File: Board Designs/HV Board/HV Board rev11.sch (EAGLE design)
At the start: 73 parts, among them IC1 OKI-78SR-5, IC2 NE5532SOIC

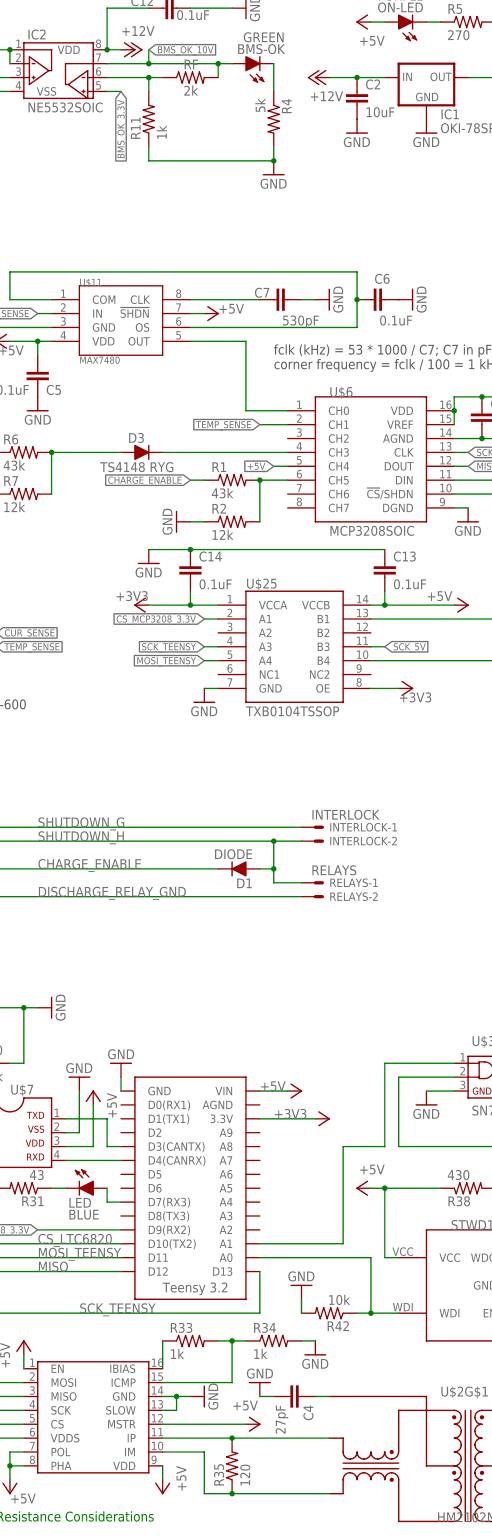
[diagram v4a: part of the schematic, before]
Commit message: HV Board rev11: comp hardware - removed extra isoSPI resistor, changed LED resistor value
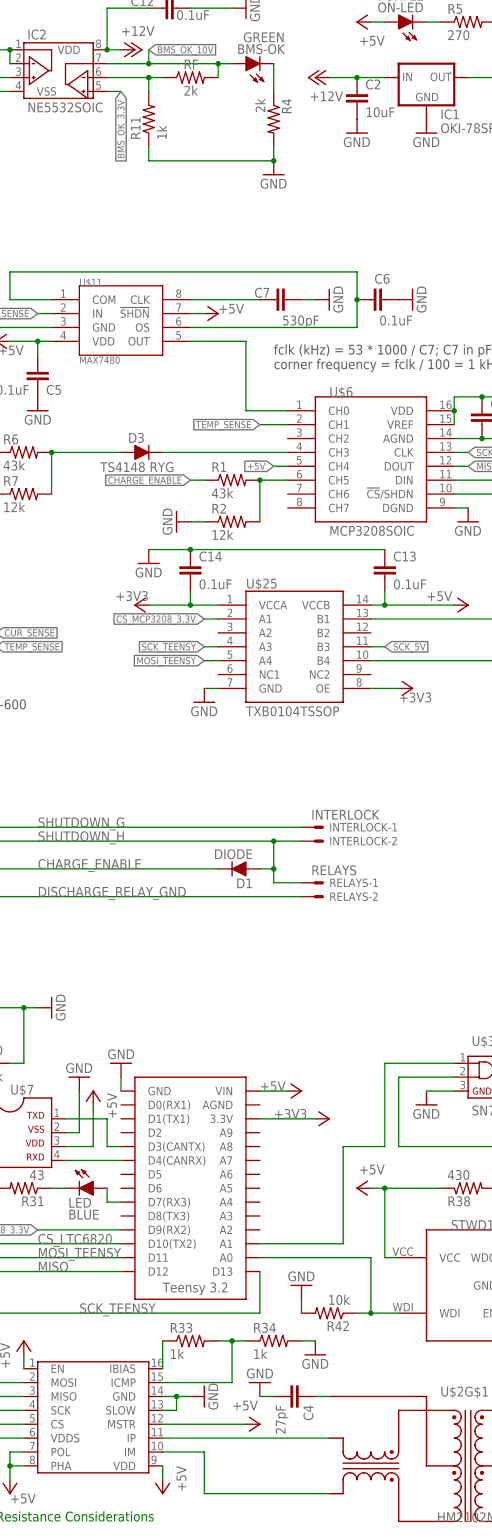
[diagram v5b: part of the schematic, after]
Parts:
- removed R35: 120, HyTechDevices:RESISTOR0805-RES
- R4: value 5k -> 2k
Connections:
- net IM: no longer R35.1
- net IP: no longer R35.2
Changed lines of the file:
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@@
 <part name="BMS-OK" library="HyTechDevices" deviceset="LED" device="-0805" value="GREEN"/>
 <part name="R3" library="HyTechDevices" deviceset="RESISTOR" device="0805-RES" value="820"/>
-<part name="R4" library="HyTechDevices" deviceset="RESISTOR" device="0805-RES" value="5k"/>
+<part name="R4" library="HyTechDevices" deviceset="RESISTOR" device="0805-RES" value="2k"/>
 <part name="GND23" library="supply1" deviceset="GND" device=""/>
 <part name="GND25" library="supply1" deviceset="GND" device=""/>
@@
 <part name="GND19" library="HyTechSymbols" deviceset="GND" device=""/>
 <part name="P+18" library="supply1" deviceset="+5V" device=""/>
-<part name="R35" library="HyTechDevices" deviceset="RESISTOR" device="0805-RES" value="120"/>
 <part name="C4" library="HyTechDevices" deviceset="CAP" device="0805" value="27pF"/>
 <part name="GND22" library="HyTechSymbols" deviceset="GND" device=""/>
@@
 <attribute name="VALUE" x="86.36" y="-287.02" size="1.778" layer="96"/>
 </instance>
-<instance part="R35" gate="G$1" x="86.36" y="-297.18" smashed="yes" rot="R90">
-<attribute name="NAME" x="84.8614" y="-300.99" size="1.778" layer="95" rot="R90"/>
-<attribute name="VALUE" x="89.662" y="-300.99" size="1.778" layer="96" rot="R90"/>
-</instance>
 <instance part="C4" gate="G$1" x="96.52" y="-284.48" smashed="yes" rot="R270">
 <attribute name="NAME" x="99.441" y="-286.004" size="1.778" layer="95" rot="R270"/>
@@
 <wire x1="73.66" y1="-294.64" x2="81.28" y2="-294.64" width="0.1524" layer="91"/>
 <wire x1="81.28" y1="-294.64" x2="81.28" y2="-302.26" width="0.1524" layer="91"/>
-<pinref part="R35" gate="G$1" pin="1"/>
-<wire x1="81.28" y1="-302.26" x2="86.36" y2="-302.26" width="0.1524" layer="91"/>
-<wire x1="104.14" y1="-302.26" x2="86.36" y2="-302.26" width="0.1524" layer="91"/>
-<junction x="86.36" y="-302.26"/>
+<wire x1="104.14" y1="-302.26" x2="81.28" y2="-302.26" width="0.1524" layer="91"/>
 <pinref part="U$2" gate="G$1" pin="TD-"/>
 </segment>
@@
 <segment>
 <pinref part="U$8" gate="G$1" pin="IP"/>
-<wire x1="73.66" y1="-292.1" x2="86.36" y2="-292.1" width="0.1524" layer="91"/>
-<pinref part="R35" gate="G$1" pin="2"/>
-<wire x1="104.14" y1="-292.1" x2="86.36" y2="-292.1" width="0.1524" layer="91"/>
-<junction x="86.36" y="-292.1"/>
+<wire x1="104.14" y1="-292.1" x2="73.66" y2="-292.1" width="0.1524" layer="91"/>
 <pinref part="U$2" gate="G$1" pin="TD+"/>
 </segment>
